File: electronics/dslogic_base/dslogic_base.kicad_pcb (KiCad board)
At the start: 2 copper layers, 3 parts, among them J1 Conn_02x23_Odd_Even

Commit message: completed schematic, board layout and updated readme
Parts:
- added J2: Conn_02x08_Odd_Even, Connector_PinHeader_1.27mm:PinHeader_2x08_P1.27mm_Vertical, F.Cu at (168.9, 72.4)
- added J3: Conn_02x08_Odd_Even, Connector_PinHeader_1.27mm:PinHeader_2x08_P1.27mm_Vertical, F.Cu at (168.9, 87.0)
- J1: footprint Connector_PinHeader_1.27mm:PinHeader_2x23_P1.27mm_Horizontal -> Connector_PinHeader_1.27mm:PinHeader_2x22_P1.27mm_Vertical
- N1, N2: moved to B.Cu
- moved N1 31.0 mm to (167.0, 80.1), turned to 180 degrees
- moved N2 29.9 mm to (166.4, 76.2), turned to 180 degrees
- moved J1 28.7 mm to (160.0, 71.7), turned to 0 degrees
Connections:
- J1 pad 1: unconnected-(J1-Pad1) -> GND
- J1 pad 10: GND -> unconnected-(J1-Pad10)
- J1 pad 11: unconnected-(J1-Pad11) -> GND
- J1 pad 12: GND -> /CH04
- J1 pad 13: unconnected-(J1-Pad13) -> GND
- J1 pad 14: GND -> /CH05
- J1 pad 15: unconnected-(J1-Pad15) -> GND
- J1 pad 16: GND -> /CH06
- J1 pad 17: unconnected-(J1-Pad17) -> GND
- J1 pad 18: GND -> /CH07
- J1 pad 2: GND -> /CH00
- J1 pad 20: GND -> unconnected-(J1-Pad20)
- J1 pad 21: unconnected-(J1-Pad21) -> GND
- J1 pad 22: GND -> /CH08
- J1 pad 23: unconnected-(J1-Pad23) -> GND
- J1 pad 24: GND -> /CH09
- J1 pad 25: unconnected-(J1-Pad25) -> GND
- J1 pad 26: GND -> /CH10
- J1 pad 27: unconnected-(J1-Pad27) -> GND
- J1 pad 28: GND -> /CH11
- J1 pad 3: unconnected-(J1-Pad3) -> GND
- J1 pad 30: GND -> unconnected-(J1-Pad30)
- J1 pad 31: unconnected-(J1-Pad31) -> GND
- J1 pad 32: GND -> /CH12
- J1 pad 33: unconnected-(J1-Pad33) -> GND
- J1 pad 34: GND -> /CH13
- J1 pad 35: unconnected-(J1-Pad35) -> GND
- J1 pad 36: GND -> /CH14
- J1 pad 37: unconnected-(J1-Pad37) -> GND
- J1 pad 38: GND -> /CH15
- J1 pad 4: GND -> /CH01
- J1 pad 40: GND -> unconnected-(J1-Pad40)
- J1 pad 41: unconnected-(J1-Pad41) -> GND
- J1 pad 42: GND -> unconnected-(J1-Pad42)
- J1 pad 43: unconnected-(J1-Pad43) -> GND
- J1 pad 44: GND -> unconnected-(J1-Pad44)
- J1 pad 5: unconnected-(J1-Pad5) -> GND
- J1 pad 6: GND -> /CH02
- J1 pad 7: unconnected-(J1-Pad7) -> GND
- J1 pad 8: GND -> /CH03
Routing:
- net /CH09: track 0.00 -> 8.67 mm
- net /CH08: track 0.00 -> 8.67 mm
- net /CH11: track 0.00 -> 8.67 mm
- net /CH10: track 0.00 -> 8.67 mm
- net /CH15: track 0.00 -> 8.14 mm
- net /CH12: track 0.00 -> 8.14 mm
- net /CH14: track 0.00 -> 8.14 mm
- net /CH13: track 0.00 -> 8.14 mm
- net /CH06: track 0.00 -> 7.88 mm
- net /CH04: track 0.00 -> 7.88 mm
- net /CH07: track 0.00 -> 7.88 mm
- net /CH05: track 0.00 -> 7.88 mm
- net /CH02: track 0.00 -> 7.88 mm
- net /CH03: track 0.00 -> 7.88 mm
- net /CH00: track 0.00 -> 7.88 mm
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- added copper zone on B.Cu, net GND
- added copper zone on F.Cu, net GND
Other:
- board outline added: 15.2 x 30.5 mm
- board text added: "CH0-7"
- board text added: "CH8-15"

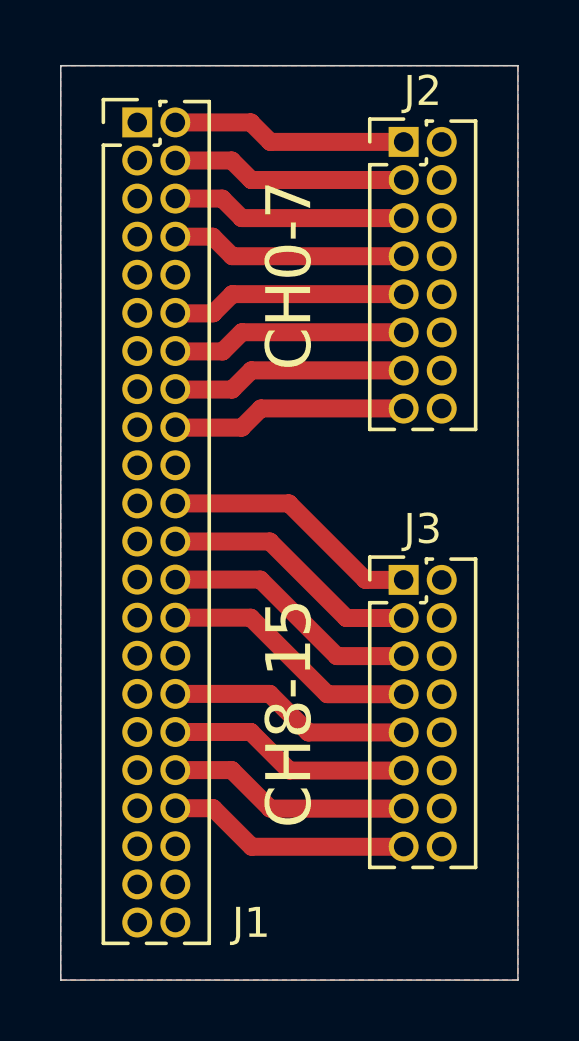
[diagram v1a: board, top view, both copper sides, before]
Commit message: added some coplanar waveguides
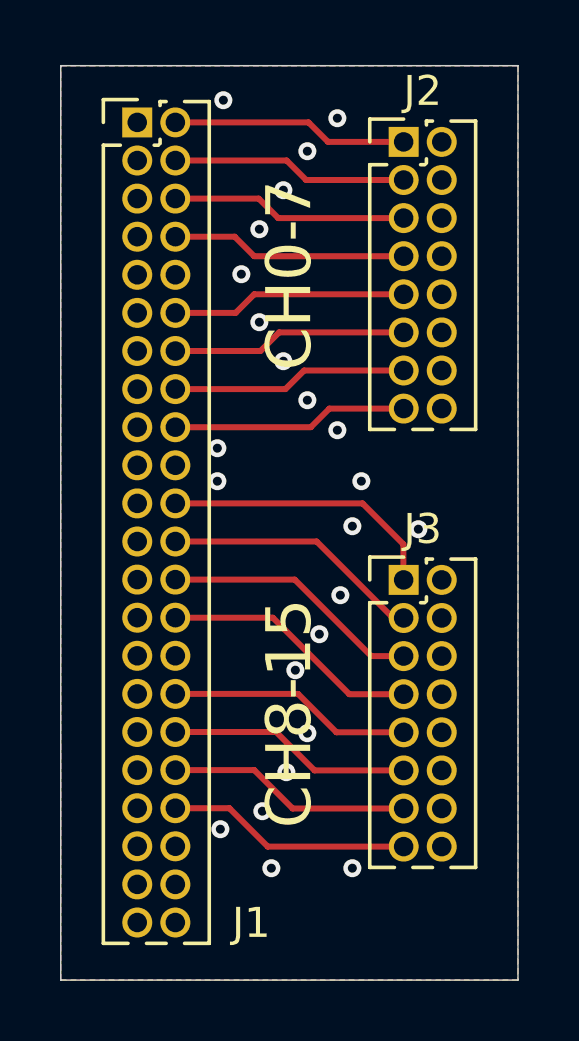
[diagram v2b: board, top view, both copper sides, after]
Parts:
- moved N1 12.0 mm to (165.4, 92.0), turned to -90 degrees
- moved N2 7.80 mm to (166.1, 84.0), turned to 90 degrees
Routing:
- net /CH08: track 8.67 -> 9.38 mm
- net GND: vias 0 -> 24

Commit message: updated versionnumber and reviewed
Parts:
- N1: value 20220923 -> 20221009
- moved N2 0.50 mm to (165.6, 84.0)
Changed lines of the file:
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@@
       (effects (font (size 1 1) (thickness 0.15)) (justify mirror))
     )
-    (fp_text value "20220923" (at 0.8 0.1 90) (layer "B.SilkS")
+    (fp_text value "20221009" (at 0.8 0.1 90) (layer "B.SilkS")
       (effects (font (size 0.8 0.8) (thickness 0.15)) (justify mirror))
     )
@@
   )
   (footprint "Symbol:OSHW-Symbol_6.7x6mm_SilkScreen" (layer "B.Cu")
-    (at 166.1 84 90)
+    (at 165.6 84 90)
     (descr "Open Source Hardware Symbol")
     (tags "Logo Symbol OSHW")
